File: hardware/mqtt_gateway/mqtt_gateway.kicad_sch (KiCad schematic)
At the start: 54 parts, among them J1 awesome:RJ45-CAN, J3 RJ45_Amphenol_RJMG1BD3B8K1ANR, J4 WAGO250-204, Q1 BC847, Q2 BC847, U1 wuerthDebug6, U2 LD1117S33TR_SOT223, U3 PESD2CAN, U4 MCP2562-E-SN, U6 ESP32-WROOM-32, U7 LAN8720A

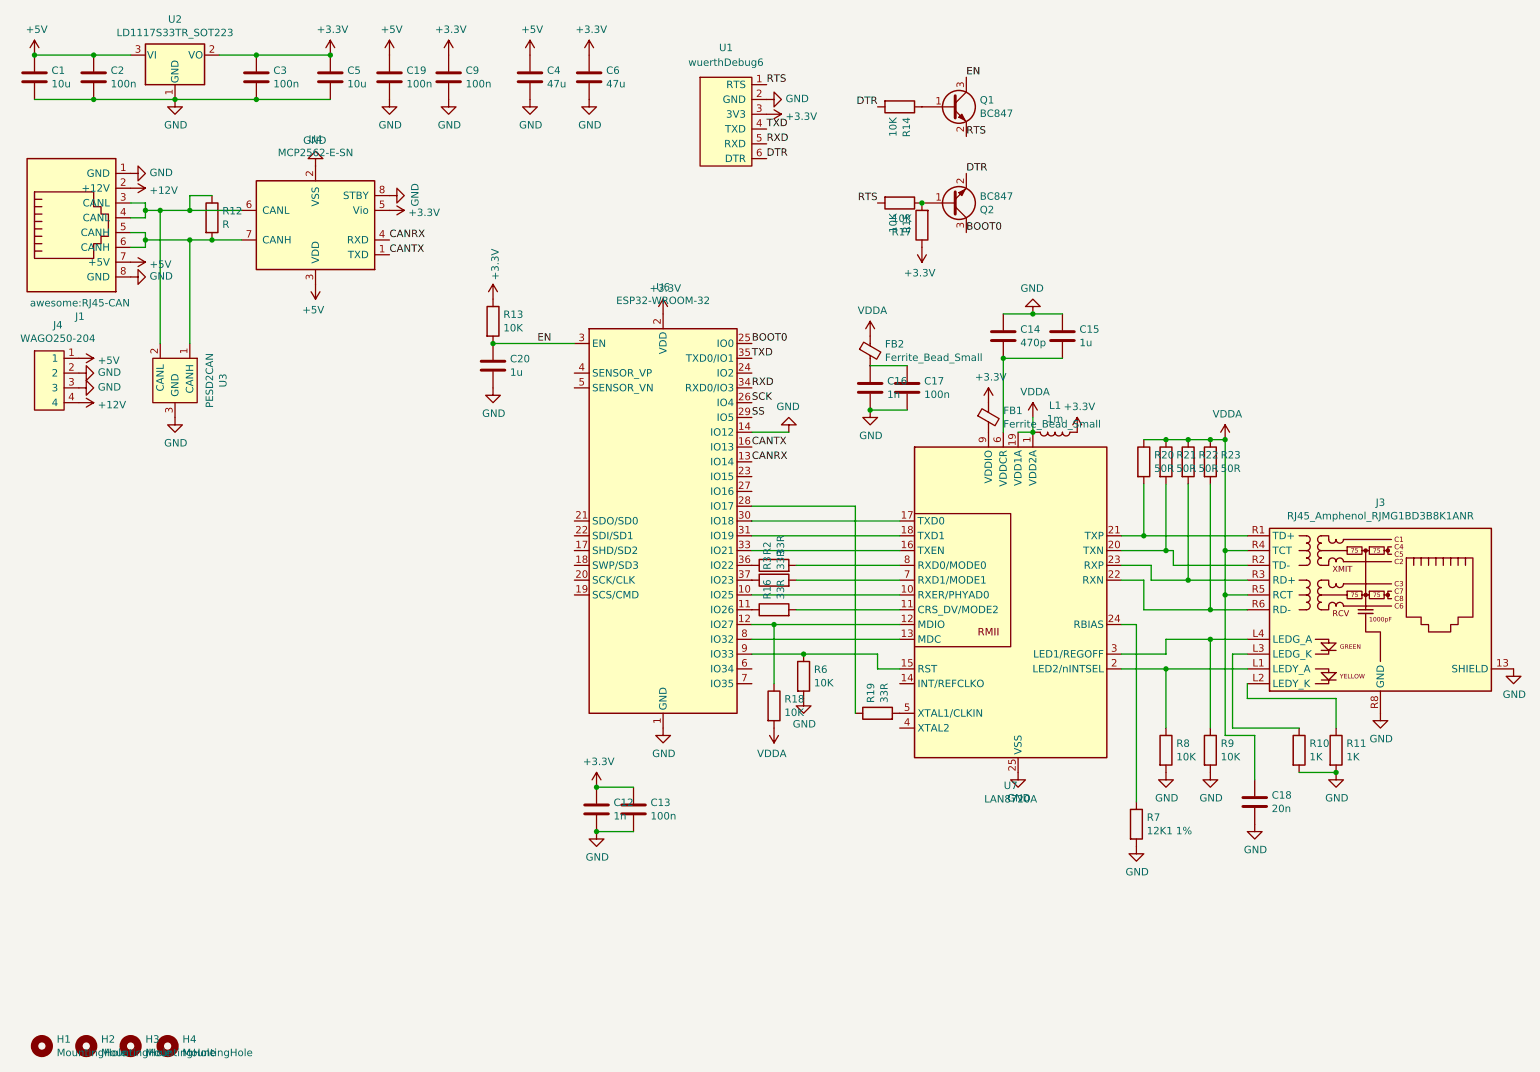
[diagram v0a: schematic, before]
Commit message: feat: Switch to 4 layer stackup
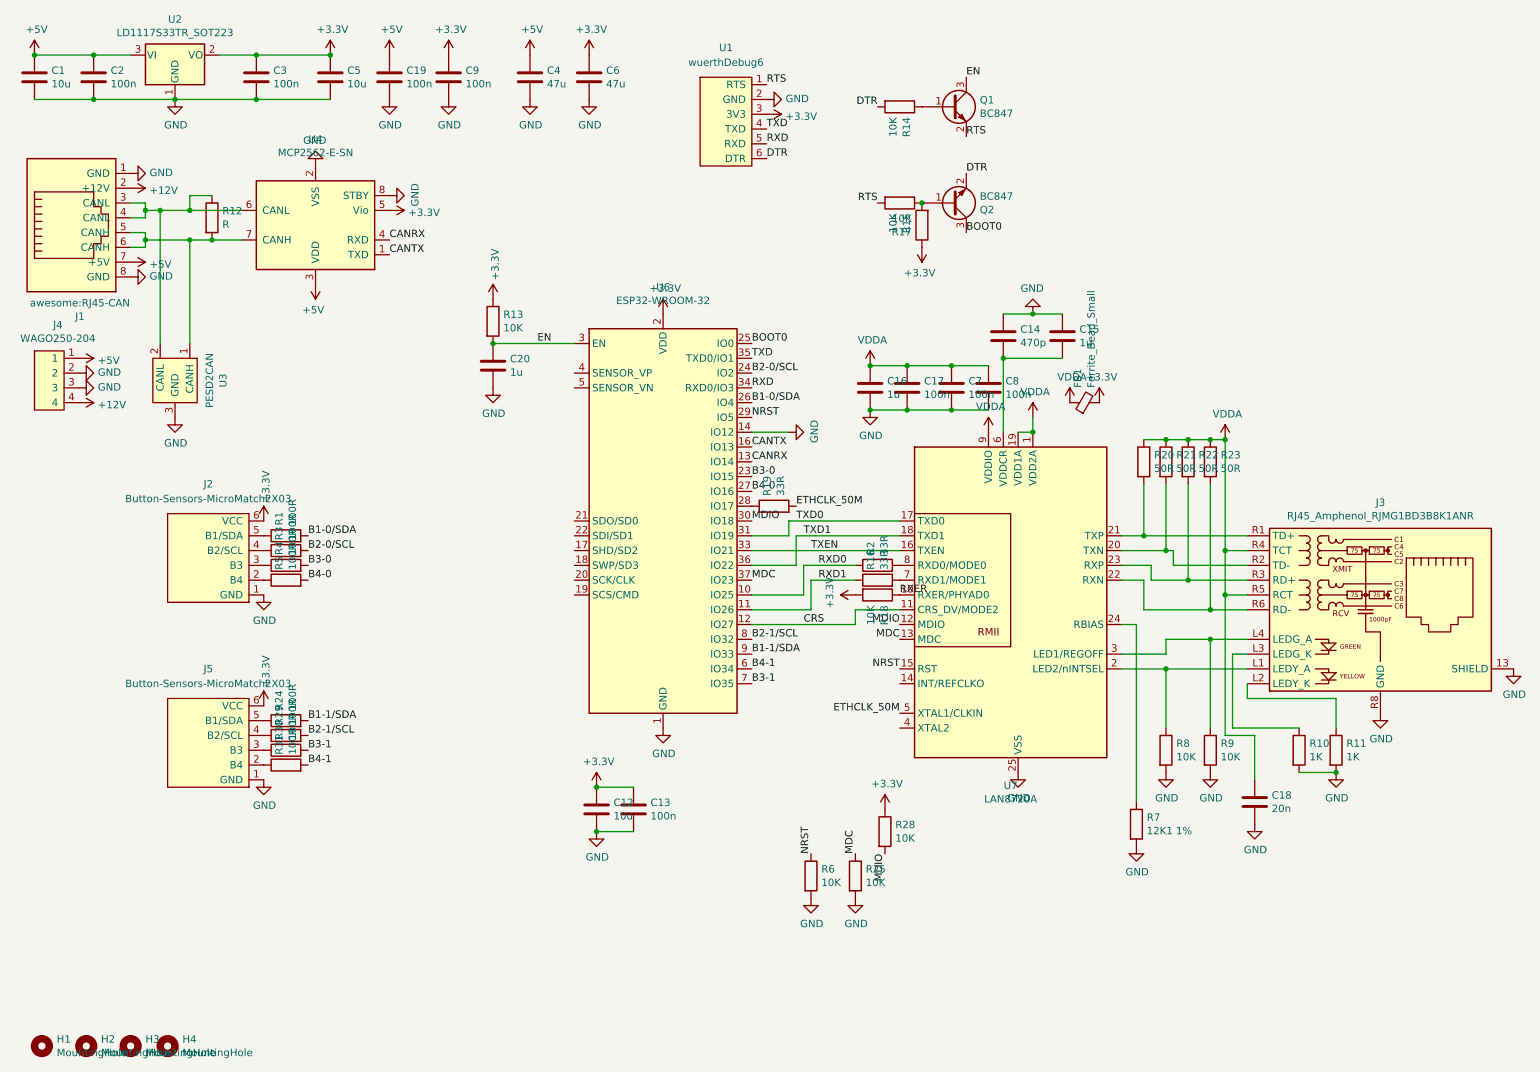
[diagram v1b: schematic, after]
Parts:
- removed FB2: Ferrite_Bead_Small, Capacitor_SMD:C_0805_2012Metric_Pad1.18x1.45mm_HandSolder, symbol Device:FerriteBead_Small
- removed L1: 1m, Inductor_SMD:L_1210_3225Metric_Pad1.42x2.65mm_HandSolder, symbol Device:L
- added C7, C8: 100n, Capacitor_SMD:C_0402_1005Metric_Pad0.74x0.62mm_HandSolder, symbol Device:C
- added J2, J5: Button-Sensors-MicroMatch2X03, awesome:02x03MicroMatch, symbol awesome:Button-Sensors-MicroMatch2X03
- added R1, R24, R29, R30, R31, R4, R5: 100R, Resistor_SMD:R_0603_1608Metric_Pad0.98x0.95mm_HandSolder, symbol Device:R
- added R25, R28: 10K, Resistor_SMD:R_0603_1608Metric_Pad0.98x0.95mm_HandSolder, symbol Device:R
- C12: value 1n -> 10u
- C14, C15, C17: footprint Capacitor_SMD:C_0603_1608Metric_Pad1.08x0.95mm_HandSolder -> Capacitor_SMD:C_0402_1005Metric_Pad0.74x0.62mm_HandSolder
- C16: value 1n -> 1u; footprint Capacitor_SMD:C_0603_1608Metric_Pad1.08x0.95mm_HandSolder -> Capacitor_SMD:C_0402_1005Metric_Pad0.74x0.62mm_HandSolder
- R16, R18, R2: footprint Resistor_SMD:R_0603_1608Metric_Pad0.98x0.95mm_HandSolder -> Resistor_SMD:R_0402_1005Metric_Pad0.72x0.64mm_HandSolder
- R3: value 33R -> 100R
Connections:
- net SS is gone; now on net NRST: U6.29 (IO5)
- net +3.3V: now also FB1.2, R18.2, J2.6 (VCC), J5.6 (VCC), R28.1; no longer FB1.1
- net GND: now also C7.2, C8.2, J2.1 (GND), J5.1 (GND), R25.2
- net VDDA: now also C16.1, C17.1, FB1.1, U7.9 (VDDIO), C7.1, C8.1; no longer R18.2
- net RXD0: now reaches U6.10 (IO25)
- net RXD0: now also R2.1; no longer U7.10 (RXER/PHYAD0)
- net RXD1: now reaches R16.1, U6.11 (IO26)
- net B3-0: now reaches U6.23 (IO15)
- net B3-0: now also R4.2
- net B2-0/SCL: now reaches U6.24 (IO2)
- net B2-0/SCL: now also R3.2
- net B4-0: now reaches U6.27 (IO16)
- net B4-0: now also R5.2
- net MDIO: now reaches U6.30 (IO18)
- net MDIO: now also U7.12 (MDIO), R28.2; no longer U7.17 (TXD0)
- net TXD0: now reaches U6.31 (IO19)
- net TXD0: now also U7.17 (TXD0); no longer U7.18 (TXD1)
- net TXEN: now reaches U6.33 (IO21), U7.16 (TXEN)
- net TXD1: now reaches U6.36 (IO22)
- net TXD1: now also U7.18 (TXD1); no longer R2.1
- net at R3.1: now also J2.4 (B2/SCL); no longer U6.37 (IO23)
- net B4-1: now reaches U6.6 (IO34)
- net B4-1: now also R31.2
- net B3-1: now reaches U6.7 (IO35)
- net B3-1: now also R30.2
- net B2-1/SCL: now reaches U6.8 (IO32)
- net B2-1/SCL: now also R29.2; no longer U7.13 (MDC)
- net NRST: now reaches R6.1, U7.15 (RST)
- net NRST: no longer U6.9 (IO33)
- net at R16.2: now also U7.7 (RXD1/MODE1); no longer U7.11 (CRS_DV/MODE2)
- net ETHCLK_50M: now reaches R19.2, U7.5 (XTAL1/CLKIN)
- net SCK renamed B1-0/SDA
- net B1-0/SDA: now also R1.2
- new net: J5.5 (B1/SDA), R24.1
- new net: J5.2 (B4), R31.1
- new net: J5.3 (B3), R30.1
- new net: J5.4 (B2/SCL), R29.1
- new net: J2.5 (B1/SDA), R1.1
- new net: J2.3 (B3), R4.1
- new net: J2.2 (B4), R5.1
- new net B1-1/SDA: R24.2, U6.9 (IO33)
- new net CRS: U6.12 (IO27), U7.11 (CRS_DV/MODE2)
- new net MDC: R25.1, U6.37 (IO23), U7.13 (MDC)
- new net RXER: R18.1, U7.10 (RXER/PHYAD0)
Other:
- moved on the sheet: FB1, R16, R18, R19, R2, R6

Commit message: feat: change PCB debug to EN/BOOT0
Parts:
- removed Q1, Q2: BC847, Package_TO_SOT_SMD:SOT-23, symbol Transistor_BJT:BC847
- removed R14, R15, R17: 10K, Resistor_SMD:R_0603_1608Metric_Pad0.98x0.95mm_HandSolder, symbol Device:R
- added R26, R27, R32, R33: 2K2, Resistor_SMD:R_0603_1608Metric_Pad0.98x0.95mm_HandSolder, symbol Device:R
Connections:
- net DTR is gone; now on net BOOT0: U1.6 (BOOT0)
- net RTS is gone; now on net EN: U1.1 (EN)
- net +3.3V: now also J2.1 (VCC), J5.1 (VCC), R26.1, R27.1, R32.1, R33.1; no longer J2.6 (VCC), J5.6 (VCC)
- net B1-0/SDA: now also R26.2
- net B1-1/SDA: now also R27.2
- net B2-0/SCL: now also R32.2
- net B2-1/SCL: now also R33.2
- net GND: now also J2.6 (GND), J5.6 (GND); no longer J2.1 (GND), J5.1 (GND)
- net at R24.1: now also J5.2 (B1/SDA); no longer J5.5 (B1/SDA)
- net at R31.1: now also J5.5 (B4); no longer J5.2 (B4)
- net at J5.3 (B2/SCL): now also R29.1; no longer R30.1
- net at J5.4 (B3): now also R30.1; no longer R29.1
- net at R1.1: now also J2.2 (B1/SDA); no longer J2.5 (B1/SDA)
- net at R4.1: now also J2.4 (B3); no longer J2.3 (B3)
- net at R5.1: now also J2.5 (B4); no longer J2.2 (B4)
- net at R3.1: now also J2.3 (B2/SCL); no longer J2.4 (B2/SCL)

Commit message: feat: Add fab export options for all pcbs
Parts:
- FB1: footprint Capacitor_SMD:C_0805_2012Metric_Pad1.18x1.45mm_HandSolder -> Capacitor_SMD:C_0603_1608Metric_Pad1.08x0.95mm_HandSolder
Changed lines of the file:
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@@
       (effects (font (size 1.27 1.27)) (justify left))
     )
-    (property "Footprint" "Capacitor_SMD:C_0805_2012Metric_Pad1.18x1.45mm_HandSolder" (id 2) (at 198.12 84.328 90)
+    (property "Footprint" "Capacitor_SMD:C_0603_1608Metric_Pad1.08x0.95mm_HandSolder" (id 2) (at 198.12 84.328 90)
       (effects (font (size 1.27 1.27)) hide)
     )
@@
     )
     (path "/00000000-0000-0000-0000-00006082645b"
-      (reference "FB1") (unit 1) (value "Ferrite_Bead_Small") (footprint "Capacitor_SMD:C_0805_2012Metric_Pad1.18x1.45mm_HandSolder")
+      (reference "FB1") (unit 1) (value "Ferrite_Bead_Small") (footprint "Capacitor_SMD:C_0603_1608Metric_Pad1.08x0.95mm_HandSolder")
     )
     (path "/00000000-0000-0000-0000-000060c7234e"

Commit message: feat: Prepare mqtt gateway 3.0
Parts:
- removed C17: 100n, Capacitor_SMD:C_0402_1005Metric_Pad0.74x0.62mm_HandSolder, symbol Device:C
- removed R18: 10K, Resistor_SMD:R_0402_1005Metric_Pad0.72x0.64mm_HandSolder, symbol Device:R
- removed R7: 12K1 1%, Resistor_SMD:R_0603_1608Metric_Pad0.98x0.95mm_HandSolder, symbol Device:R
- removed U7: LAN8720A, Package_DFN_QFN:QFN-24-1EP_4x4mm_P0.5mm_EP2.6x2.6mm, symbol Interface_Ethernet:LAN8720A
- added C10: 22u, Capacitor_SMD:C_0805_2012Metric_Pad1.18x1.45mm_HandSolder, symbol Device:C
- added C11: 100n, Capacitor_SMD:C_0603_1608Metric_Pad1.08x0.95mm_HandSolder, symbol Device:C
- added R35: 10K, Resistor_SMD:R_0603_1608Metric_Pad0.98x0.95mm_HandSolder, symbol Device:R
- added U5: KSZ8081MLX, Package_QFP:LQFP-48_7x7mm_P0.5mm, symbol Interface_Ethernet:KSZ8081MLX
- C14: value 470p -> 100n; footprint Capacitor_SMD:C_0402_1005Metric_Pad0.74x0.62mm_HandSolder -> Capacitor_SMD:C_0603_1608Metric_Pad1.08x0.95mm_HandSolder
- C15: value 1u -> 2u2; footprint Capacitor_SMD:C_0402_1005Metric_Pad0.74x0.62mm_HandSolder -> Capacitor_SMD:C_0603_1608Metric_Pad1.08x0.95mm_HandSolder
- C16: value 1u -> 22u; footprint Capacitor_SMD:C_0402_1005Metric_Pad0.74x0.62mm_HandSolder -> Capacitor_SMD:C_0805_2012Metric_Pad1.18x1.45mm_HandSolder
- C7, C8: footprint Capacitor_SMD:C_0402_1005Metric_Pad0.74x0.62mm_HandSolder -> Capacitor_SMD:C_0603_1608Metric_Pad1.08x0.95mm_HandSolder
- FB1: value Ferrite_Bead_Small -> BLM18KG331SH1D
- R10, R11: value 1K -> 220R
- R16, R2: footprint Resistor_SMD:R_0402_1005Metric_Pad0.72x0.64mm_HandSolder -> Resistor_SMD:R_0603_1608Metric_Pad0.98x0.95mm_HandSolder
- R8, R9: value 10K -> 4K7
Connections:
- net +3.3V: now also R10.1, R11.1, R8.2, R9.2, C10.1, C11.2, U5.25 (VDDIO)
- net B4-0: now also U6.28 (IO17); no longer U6.27 (IO16)
- net CRS: now also R35.1, U5.41 (CRS/CONFIG1)
- net ETHCLK_50M: now also U5.15 (XI)
- net GND: now also C16.1, C7.1, C10.2, C11.1, R35.2, U5.1 (GND), U5.13 (GND), U5.17 (GND), U5.2 (GND), U5.24 (GND), U5.3 (GND), U5.30 (GND), U5.37 (GND); no longer C16.2, C7.2, R10.2, R11.2, R8.2, R9.2
- net MDC: now also U5.19 (MDC)
- net MDIO: now also U5.18 (MDIO)
- net NRST: now also U5.47 (~{RST})
- net TXD0: now also U5.35 (TXD0)
- net TXD1: now also U5.36 (TXD1)
- net TXEN: now also U5.34 (TXEN)
- net VDDA: now also C16.2, U5.7 (VDDA_3.3); no longer C16.1, C7.1
- net at R19.1: now also U6.27 (IO16); no longer U6.28 (IO17)
- net at J3.L1 (LEDY_A): now also R11.2; no longer R8.1
- net at J3.L2 (LEDY_K): now also R8.1, U5.43 (LED1/SPEED); no longer R11.1
- net at J3.L3 (LEDG_K): now also R9.1, U5.42 (LED0/NWAYEN); no longer R10.1
- net at J3.L4 (LEDG_A): now also R10.2; no longer R9.1
- net at J3.R1 (TD+), R20.2: now also U5.12 (TXP)
- net at J3.R2 (TD-), R21.2: now also U5.11 (TXM)
- net at J3.R3 (RD+), R22.2: now also U5.10 (RXP)
- net at J3.R6 (RD-), R23.2: now also U5.9 (RXM)
- net at C14.2, C15.2: now also C7.2, U5.31 (VDD_1.2), U5.4 (VDD_1.2)
- net at R16.2: now also U5.22 (RXD1/PHYAD2)
- net at R2.2: now also U5.23 (RXD0/DUPLEX)
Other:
- moved on the sheet: C14, C15, C16, C18, C7, C8, FB1, R10, R11, R16, R19, R2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
